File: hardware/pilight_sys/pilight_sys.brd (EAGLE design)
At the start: 71.1 x 43.6 mm, 23 parts, among them IC1 TINY13-20PU, IC2 74ABT125DB, P1 B2P-VH, P2 B2P-VH, P3 B4B-PH-K, P4 B2B-PH-K, P5 B2B-PH-K, P6 B2P-VH, P7 B2B-PH-K, Q1 IRLB8748PBF-VER

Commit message: Finished v1 eagle designs
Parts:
- P3: value B4B-PH-K -> B2P-VH; device con-jst-ph:B4B-PH-K -> con-jst-vh:B2P-VH
- P6: value B2P-VH -> B2B-PH-K; device con-jst-vh:B2P-VH -> con-jst-ph:B2B-PH-K
- P7: value B2B-PH-K -> B4B-PH-K; device con-jst-ph:B2B-PH-K -> con-jst-ph:B4B-PH-K
- moved P6 34.4 mm to (31.3, 4.49), turned to 0 degrees
- moved P3 32.2 mm to (43.5, 36.6), turned to 180 degrees
- moved P7 28.7 mm to (42.2, 4.49)
- moved P4 17.8 mm to (13.5, 4.49)
- moved C1 12.2 mm to (14.0, 26.5)
- moved R1 2.54 mm to (25.4, 16.8)
- moved R2 2.54 mm to (25.4, 13.0)
- moved R3 2.54 mm to (31.3, 13.0)
- moved KK1 0.51 mm to (55.4, 21.9)
- moved Q1 0.51 mm to (55.4, 21.9)
- turned C2 to 0 degrees
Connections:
- net GND: now also P7.1; no longer P3.1
- net N$1: now also P4.1; no longer P7.1
- net N$13: now also P7.2; no longer P3.2
- net N$2: now also P4.2; no longer P7.2
- net N$5: now also P3.2; no longer P6.2
- net N$6: now also P6.1; no longer P4.1
- net N$7: now also P6.2; no longer P4.2
- net N$8: now also P7.3; no longer P3.3
- net VCC: now also P3.1, P7.4; no longer P3.4, P6.1
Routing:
- net GND: track 15.3 -> 8.93 mm, vias 5 -> 6
- net N$6: track 13.7 -> 16.2 mm
- net N$7: track 5.99 -> 8.53 mm
- net N$12: track 13.0 -> 10.5 mm
- net N$11: track 7.53 -> 5.18 mm
- net N$9: track 15.2 -> 14.6 mm
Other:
- board text added: "CLK"
- board text added: "CTRL"
- board text added: "DATA"
- board text added: "EXT_PW"
- board text added: "IN"
- board text added: "LED+"
- board text added: "LED_PW"
- board text added: "OUT"
- board text added: "PW"
- board text added: "Rev. 1"
- board text removed: "PWR"
- board text removed: "PWR_EXT"
- board text removed: "PWR_LED"

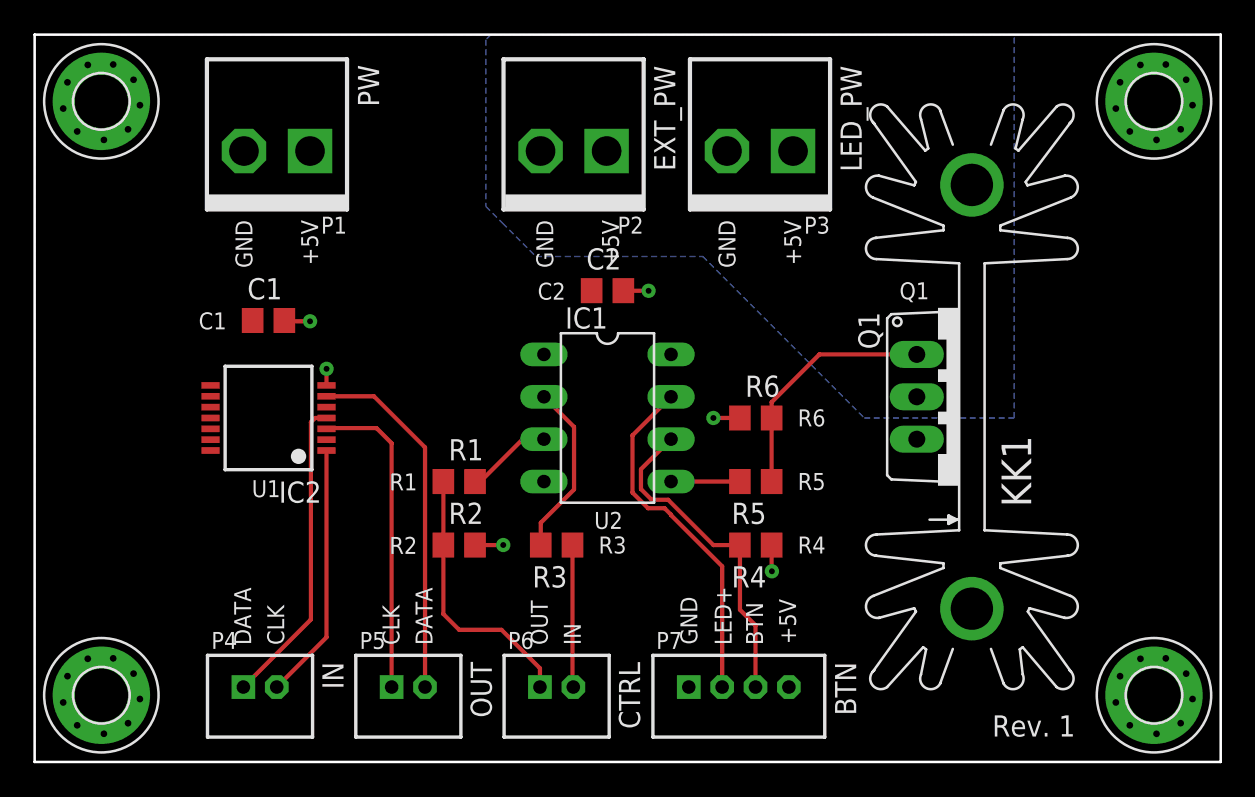
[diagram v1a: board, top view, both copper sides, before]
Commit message: Fix bug in circuit (3-state buffer)
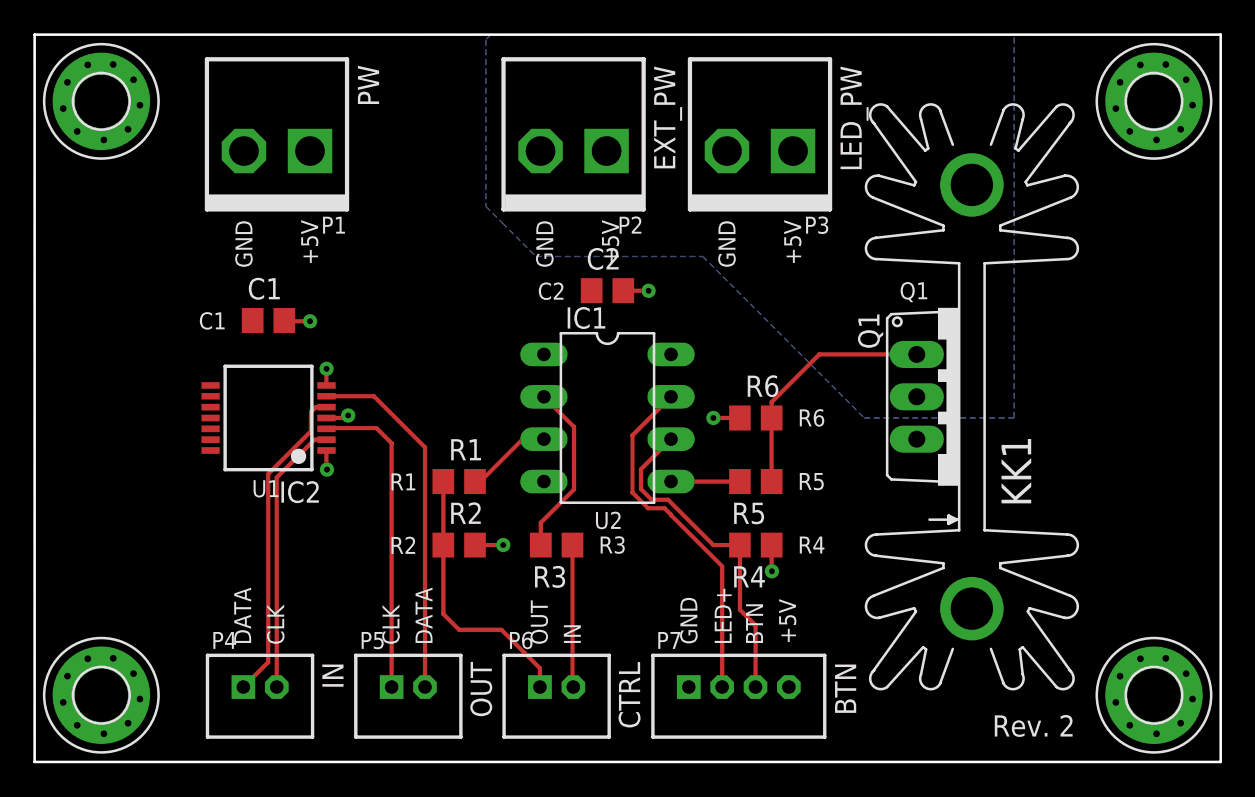
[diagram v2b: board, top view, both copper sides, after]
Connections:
- net GND: now also IC2.1, IC2.4
- net N$1: now also IC2.5; no longer IC2.4
- net N$2: now also IC2.2; no longer IC2.1
- net VCC: no longer IC2.2, IC2.5
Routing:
- net GND: track 8.93 -> 11.5 mm, vias 6 -> 8
- net N$2: track 15.4 -> 16.5 mm
- net N$1: track 18.6 -> 19.2 mm
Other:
- board text added: "Rev. 2"
- board text removed: "Rev. 1"
